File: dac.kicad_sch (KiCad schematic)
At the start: 18 parts, among them J11 EPY.00.250.NTN, J13 EPY.00.250.NTN, U7 AD5754BREZ, U8 SN74AVC8T245PW

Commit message: Finish Regulator section
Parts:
- renumbered C45 to C81, C46 to C82, C41 to C83, C42 to C84, C44 to C85, C43 to C86, C47 to C87, C48 to C88, C49 to C89, C50 to C90, J13 to J10, J11 to J9, R25 to R118, R26 to R119, R28 to R120, R29 to R121, U8 to U10, U7 to U11

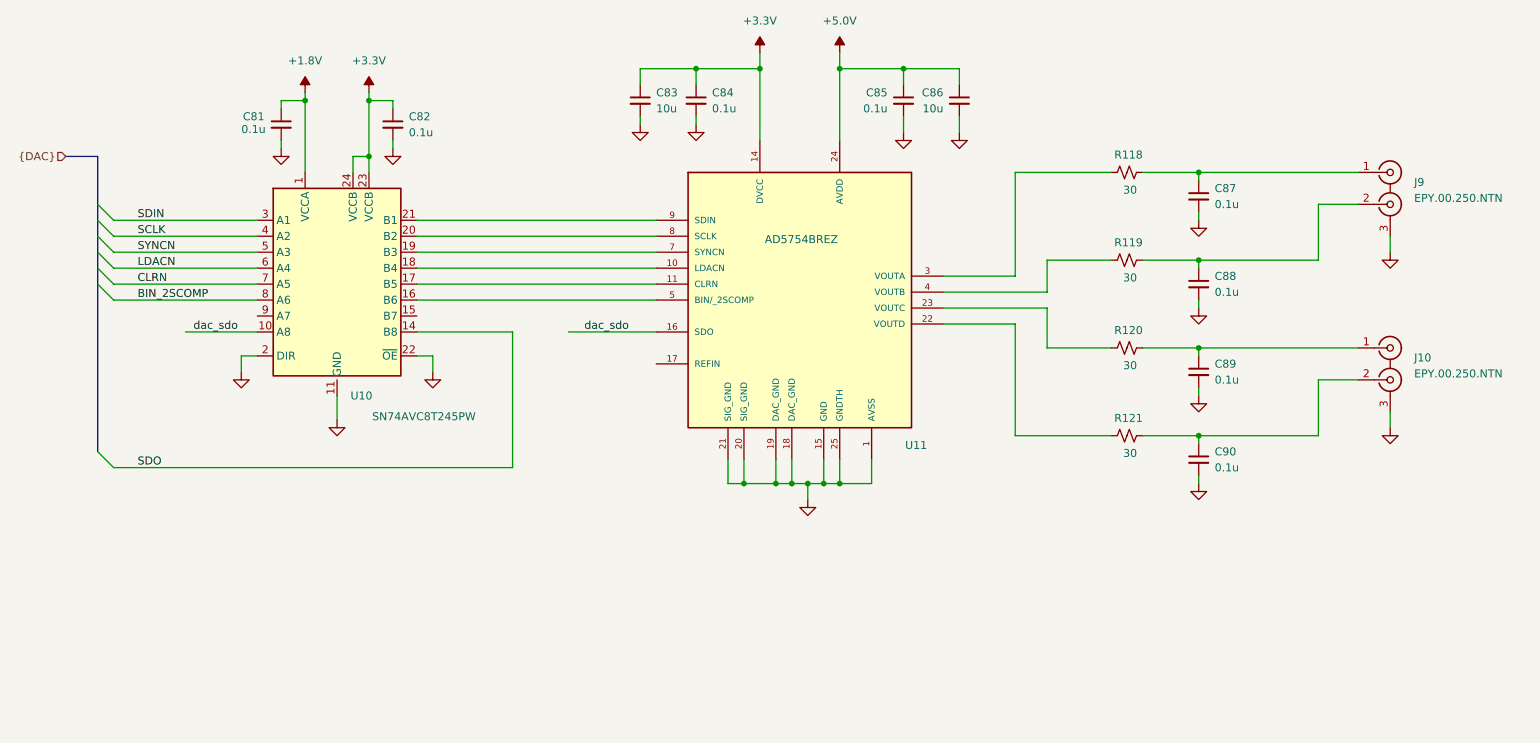
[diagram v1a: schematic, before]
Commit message: Add digital Outputs
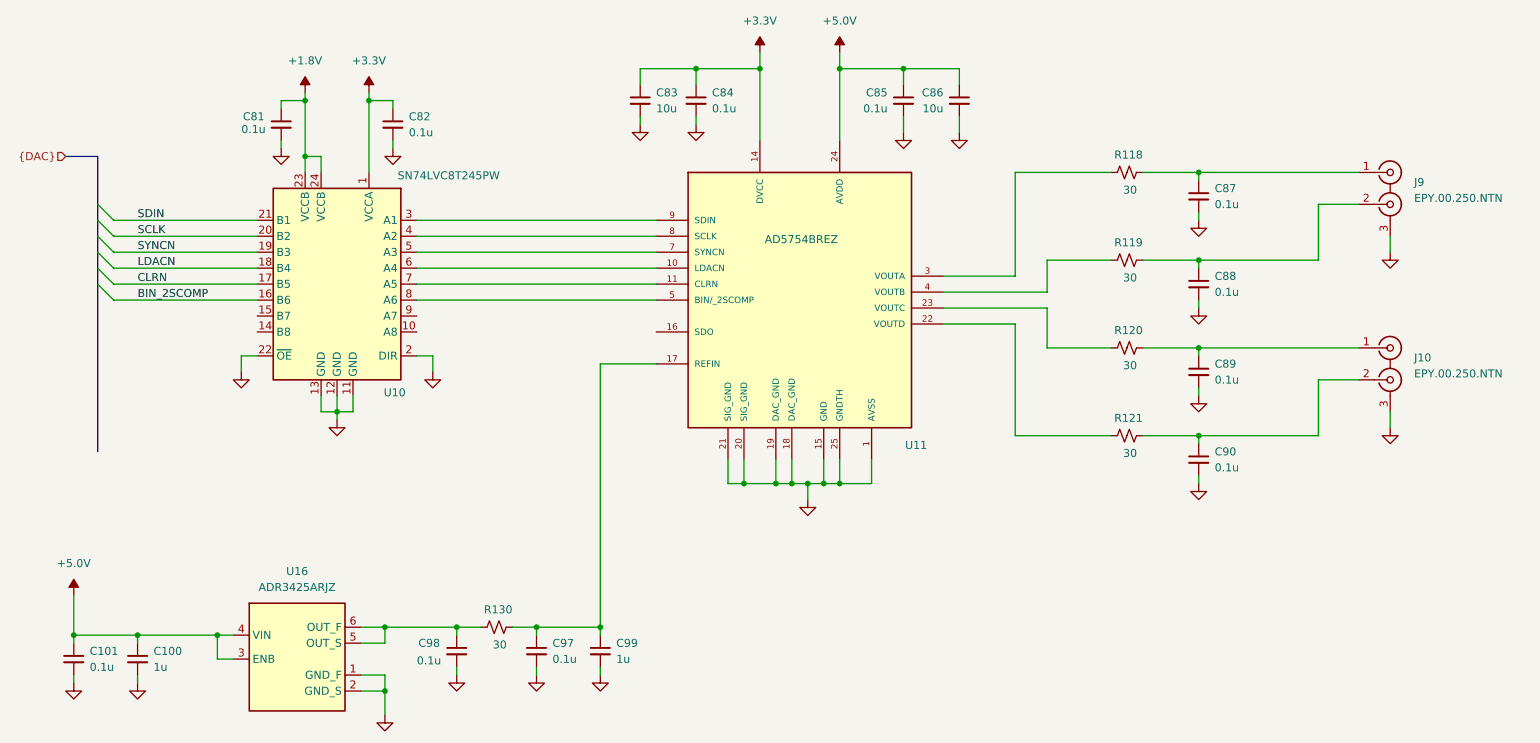
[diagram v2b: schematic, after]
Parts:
- removed U10: SN74AVC8T245PW, Package_SO:TSSOP-24_4.4x7.8mm_P0.65mm, symbol My Symbols:SN74AVC8T245PW
- added C100, C99: 1u, Capacitor_SMD:C_0603_1608Metric, symbol Device:C_Small
- added C101, C97, C98: 0.1u, Capacitor_SMD:C_0603_1608Metric, symbol Device:C_Small
- added R130: 30, Resistor_SMD:R_0603_1608Metric, symbol Device:R_Small_US
- added U10: SN74LVC8T245PW, Package_SO:TSSOP-24_4.4x7.8mm_P0.65mm, symbol My Symbols:SN74LVC8T245PW
- added U16: ADR3425ARJZ, My Footprints:SOT95P280X145-6N, symbol My Symbols:ADR3425ARJZ
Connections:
- net +1.8V: now also U10.23 (VCCB), U10.24 (VCCB)
- net +3.3V: now also U10.1 (VCCA)
- net +5.0V: now also C100.1, C101.1, U16.3 (ENB), U16.4 (VIN)
- net BIN_2SCOMP: now also U10.16 (B6)
- net CLRN: now also U10.17 (B5)
- net GND: now also C100.2, C101.2, C97.2, C98.2, C99.2, U10.11 (GND), U10.12 (GND), U10.13 (GND), U10.2 (DIR), U10.22 (~{OE}), U16.1 (GND_F), U16.2 (GND_S)
- net LDACN: now also U10.18 (B4)
- net SCLK: now also U10.20 (B2)
- net SDIN: now also U10.21 (B1)
- net SYNCN: now also U10.19 (B3)
- net at U11.5 (BIN/_2SCOMP): now also U10.8 (A6)
- net at U11.11 (CLRN): now also U10.7 (A5)
- net at U11.10 (LDACN): now also U10.6 (A4)
- net at U11.7 (SYNCN): now also U10.5 (A3)
- net at U11.8 (SCLK): now also U10.4 (A2)
- net at U11.9 (SDIN): now also U10.3 (A1)
- net at U11.17 (REFIN): now also C97.1, C99.1, R130.2
- net dac_sdo: no longer names the net of U11.16 (SDO)
- new net: C98.1, R130.1, U16.5 (OUT_S), U16.6 (OUT_F)
